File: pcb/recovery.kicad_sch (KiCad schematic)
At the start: 5 parts, among them Q1 SiS454DN

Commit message: Syncing up!
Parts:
- R11: value 1k -> 100k
- R12: value 1k -> 22k
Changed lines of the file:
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@@
 			)
 		)
-		(property "Value" "1k"
+		(property "Value" "22k"
 			(at 161.29 99.0599 0)
 			(effects
@@
 			)
 		)
-		(property "Value" "1k"
+		(property "Value" "100k"
 			(at 161.29 88.8999 0)
 			(effects

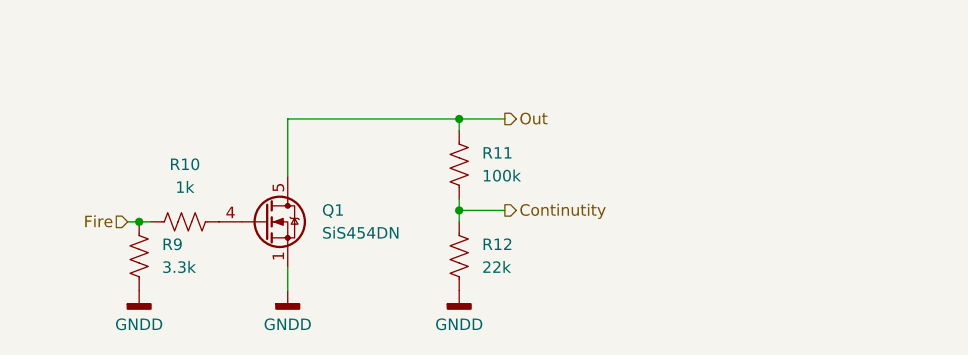
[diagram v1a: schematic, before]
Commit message: Updated Control Module Test bed schematics
Added Test points for Pyro controllers, Micro SD, and USB-C

Connected VDDUSB to 3.3V and not Vusb
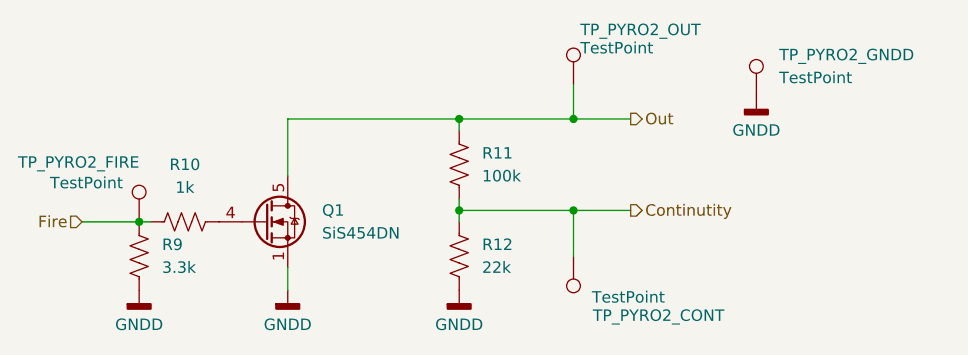
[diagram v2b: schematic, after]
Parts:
- added TP_PYRO2_CONT, TP_PYRO2_FIRE, TP_PYRO2_GNDD, TP_PYRO2_OUT: TestPoint, TestPoint:TestPoint_Loop_D2.54mm_Drill1.5mm_Beaded, symbol Connector:TestPoint
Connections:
- net Continutity: now also TP_PYRO2_CONT.1
- net Fire: now also TP_PYRO2_FIRE.1
- net GNDD: now also TP_PYRO2_GNDD.1
- net Out: now also TP_PYRO2_OUT.1

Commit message: Updated Schematics
Completed Schematics for Test Bed, updated pcb
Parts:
- renumbered R11 to R10, R12 to R11, R9 to R8, R10 to R9, TP_PYRO2_CONT to TP_PYRO2_CONT1, TP_PYRO2_FIRE to TP_PYRO2_FIRE1, TP_PYRO2_GNDD to TP_PYRO2_GNDD1, TP_PYRO2_OUT to TP_PYRO2_OUT1

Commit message: Pre-fab update
Pre fab update
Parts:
- renumbered TP_PYRO2_GNDD1 to GNDD1, TP_PYRO2_CONT1 to PYRO2_CONT1, TP_PYRO2_FIRE1 to PYRO2_FIRE1, TP_PYRO2_OUT1 to PYRO2_OUT1
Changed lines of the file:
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@@
+			)
+		)
+		(property "Sim.Device" ""
+			(at 123.19 97.79 0)
+			(effects
+				(font
+					(size 1.27 1.27)
+				)
+				(hide yes)
 			)
 		)
@@
 		(on_board yes)
 		(dnp no)
-		(property "Reference" "TP_PYRO2_CONT1"
+		(property "Reference" "PYRO2_CONT1"
 			(at 188.214 104.394 0)
 			(effects
@@
 			)
 		)
-		(pin "1"
-		)
-		(instances
-			(project "control-module"
-				(path "/ba7b4294-8d75-4b9e-892f-fb52727887ec/2c5e2862-ff08-4e6b-88a7-19e0713fdfd8"
-					(reference "TP_PYRO2_CONT1")
-					(unit 1)
-				)
-				(path "/ba7b4294-8d75-4b9e-892f-fb52727887ec/39cd510b-4c65-4a51-9a25-0e0b3aa6fc74"
-					(reference "TP_PYRO1_CONT1")
+		(property "Sim.Device" ""
+			(at 171.45 97.79 0)
+			(effects
+				(font
+					(size 1.27 1.27)
+				)
+				(hide yes)
+			)
+		)
+		(pin "1"
+		)
+		(instances
+			(project "control-module"
+				(path "/ba7b4294-8d75-4b9e-892f-fb52727887ec/2c5e2862-ff08-4e6b-88a7-19e0713fdfd8"
+					(reference "PYRO2_CONT1")
+					(unit 1)
+				)
+				(path "/ba7b4294-8d75-4b9e-892f-fb52727887ec/39cd510b-4c65-4a51-9a25-0e0b3aa6fc74"
+					(reference "PYRO1_CONT1")
 					(unit 1)
 				)
@@
 		(on_board yes)
 		(dnp no)
-		(property "Reference" "TP_PYRO2_OUT1"
+		(property "Reference" "PYRO2_OUT1"
 			(at 172.212 72.644 0)
 			(effects
@@
 			)
 		)
-		(pin "1"
-		)
-		(instances
-			(project "control-module"
-				(path "/ba7b4294-8d75-4b9e-892f-fb52727887ec/2c5e2862-ff08-4e6b-88a7-19e0713fdfd8"
-					(reference "TP_PYRO2_OUT1")
-					(unit 1)
-				)
-				(path "/ba7b4294-8d75-4b9e-892f-fb52727887ec/39cd510b-4c65-4a51-9a25-0e0b3aa6fc74"
-					(reference "TP_PYRO1_OUT1")
+		(property "Sim.Device" ""
+			(at 171.45 78.74 0)
+			(effects
+				(font
+					(size 1.27 1.27)
+				)
+				(hide yes)
+			)
+		)
+		(pin "1"
+		)
+		(instances
+			(project "control-module"
+				(path "/ba7b4294-8d75-4b9e-892f-fb52727887ec/2c5e2862-ff08-4e6b-88a7-19e0713fdfd8"
+					(reference "PYRO2_OUT1")
+					(unit 1)
+				)
+				(path "/ba7b4294-8d75-4b9e-892f-fb52727887ec/39cd510b-4c65-4a51-9a25-0e0b3aa6fc74"
+					(reference "PYRO1_OUT1")
 					(unit 1)
 				)
@@
 		(dnp no)
 		(fields_autoplaced yes)
-		(property "Reference" "TP_PYRO2_GNDD1"
+		(property "Reference" "GNDD1"
 			(at 194.31 75.4379 0)
 			(effects
@@
 			)
 		)
-		(pin "1"
-		)
-		(instances
-			(project "control-module"
-				(path "/ba7b4294-8d75-4b9e-892f-fb52727887ec/2c5e2862-ff08-4e6b-88a7-19e0713fdfd8"
-					(reference "TP_PYRO2_GNDD1")
-					(unit 1)
-				)
-				(path "/ba7b4294-8d75-4b9e-892f-fb52727887ec/39cd510b-4c65-4a51-9a25-0e0b3aa6fc74"
-					(reference "TP_PYRO1_GNDD1")
+		(property "Sim.Device" ""
+			(at 191.77 80.01 0)
+			(effects
+				(font
+					(size 1.27 1.27)
+				)
+				(hide yes)
+			)
+		)
+		(pin "1"
+		)
+		(instances
+			(project "control-module"
+				(path "/ba7b4294-8d75-4b9e-892f-fb52727887ec/2c5e2862-ff08-4e6b-88a7-19e0713fdfd8"
+					(reference "GNDD1")
+					(unit 1)
+				)
+				(path "/ba7b4294-8d75-4b9e-892f-fb52727887ec/39cd510b-4c65-4a51-9a25-0e0b3aa6fc74"
+					(reference "PYRO1_GNDD1")
 					(unit 1)
 				)
@@
 			)
 		)
+		(property "Sim.Device" ""
+			(at 158.75 97.79 0)
+			(effects
+				(font
+					(size 1.27 1.27)
+				)
+				(hide yes)
+			)
+		)
 		(pin "2"
 		)
@@
 		(on_board yes)
 		(dnp no)
-		(property "Reference" "TP_PYRO2_FIRE1"
+		(property "Reference" "PYRO2_FIRE1"
 			(at 109.728 87.376 0)
 			(effects
@@
 			)
 		)
-		(pin "1"
-		)
-		(instances
-			(project "control-module"
-				(path "/ba7b4294-8d75-4b9e-892f-fb52727887ec/2c5e2862-ff08-4e6b-88a7-19e0713fdfd8"
-					(reference "TP_PYRO2_FIRE1")
-					(unit 1)
-				)
-				(path "/ba7b4294-8d75-4b9e-892f-fb52727887ec/39cd510b-4c65-4a51-9a25-0e0b3aa6fc74"
-					(reference "TP_PYRO1_FIRE1")
+		(property "Sim.Device" ""
+			(at 123.19 93.98 0)
+			(effects
+				(font
+					(size 1.27 1.27)
+				)
+				(hide yes)
+			)
+		)
+		(pin "1"
+		)
+		(instances
+			(project "control-module"
+				(path "/ba7b4294-8d75-4b9e-892f-fb52727887ec/2c5e2862-ff08-4e6b-88a7-19e0713fdfd8"
+					(reference "PYRO2_FIRE1")
+					(unit 1)
+				)
+				(path "/ba7b4294-8d75-4b9e-892f-fb52727887ec/39cd510b-4c65-4a51-9a25-0e0b3aa6fc74"
+					(reference "PYRO1_FIRE1")
 					(unit 1)
 				)
@@
 			)
 		)
+		(property "Sim.Device" ""
+			(at 128.27 93.98 90)
+			(effects
+				(font
+					(size 1.27 1.27)
+				)
+				(hide yes)
+			)
+		)
 		(pin "2"
 		)
@@
 			)
 		)
+		(property "Sim.Device" ""
+			(at 137.16 93.98 0)
+			(effects
+				(font
+					(size 1.27 1.27)
+				)
+				(hide yes)
+			)
+		)
 		(pin "5"
 		)
@@
 			)
 		)
+		(property "Sim.Device" ""
+			(at 158.75 87.63 0)
+			(effects
+				(font
+					(size 1.27 1.27)
+				)
+				(hide yes)
+			)
+		)
